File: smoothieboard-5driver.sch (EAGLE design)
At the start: 309 parts, among them IC1 LPC1769, IC10 LM1117-3.3V, IC11 78L12F, IC12 A4982, IC13 R-78E-5.0, IC14 TC4427, IC15 TC4427, IC2 A4982, IC3 A4982, IC4 MCP44X1, IC5 A4982, IC6 A4982, IC9 MCP44X1, J10 POWER_JACKSMD, Q1 BSL207SP, Q10 SUD50P04-08-GE3, Q2 12MHz, Q3 25MHz, Q4 ZXMN4A06, Q5 AOT240L, Q6 AOT240L, Q7 AOT240L, Q8 ZXMN4A06, Q9 ZXMN4A06, U1 USD-SOCKETNEW, X14 USBPTH

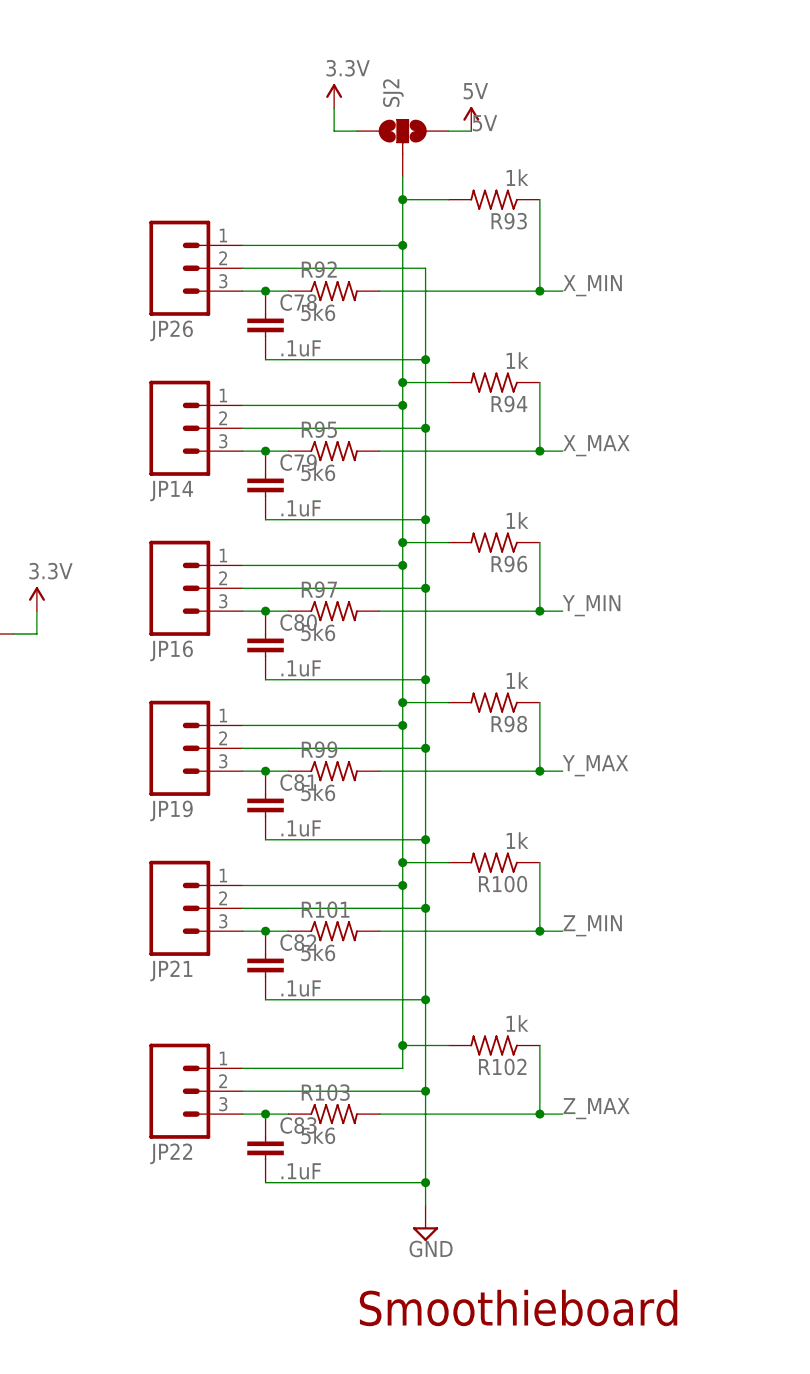
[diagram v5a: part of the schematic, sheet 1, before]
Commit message: fix endstop input ESD protection
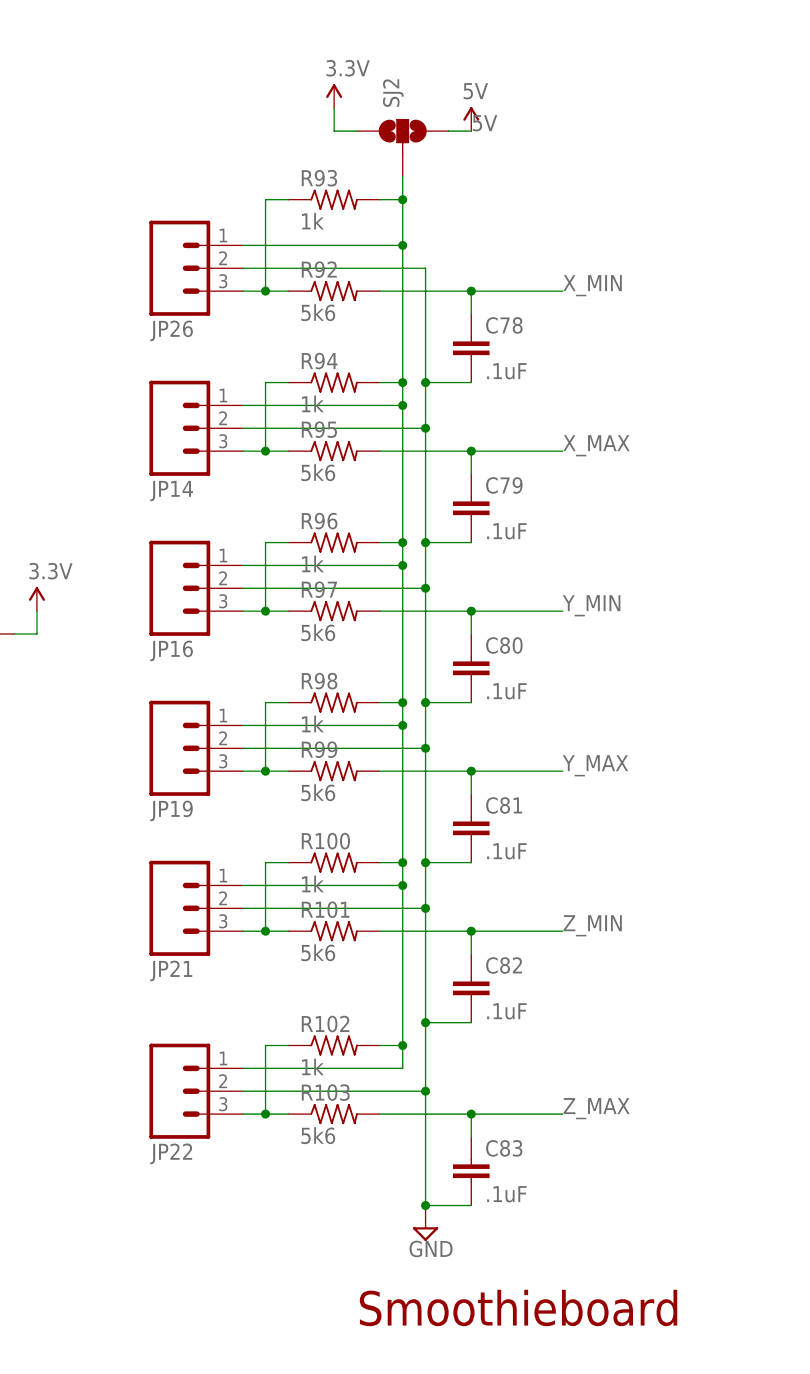
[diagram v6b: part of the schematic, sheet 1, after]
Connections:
- net N$114: now also R94.1; no longer C79.1
- net N$116: now also R96.1; no longer C80.1
- net N$117: now also R98.1; no longer C81.1
- net N$118: now also R102.1; no longer C83.1
- net N$119: now also R100.1; no longer C82.1
- net N$122: now also R93.1; no longer C78.1
- net X_MAX: now also C79.1; no longer R94.1
- net X_MIN: now also C78.1; no longer R93.1
- net Y_MAX: now also C81.1; no longer R98.1
- net Y_MIN: now also C80.1; no longer R96.1
- net Z_MAX: now also C83.1; no longer R102.1
- net Z_MIN: now also C82.1; no longer R100.1
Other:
- moved on the sheet: C78, C79, C80, C81, C82, C83, R100, R102, R93, R94, R96, R98

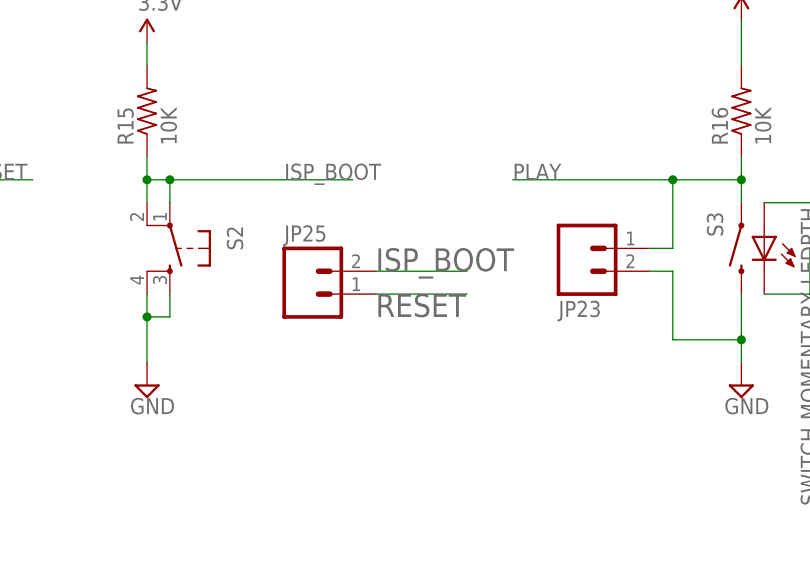
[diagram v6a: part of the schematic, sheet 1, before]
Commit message: lots of silk including pinouts on the bottom
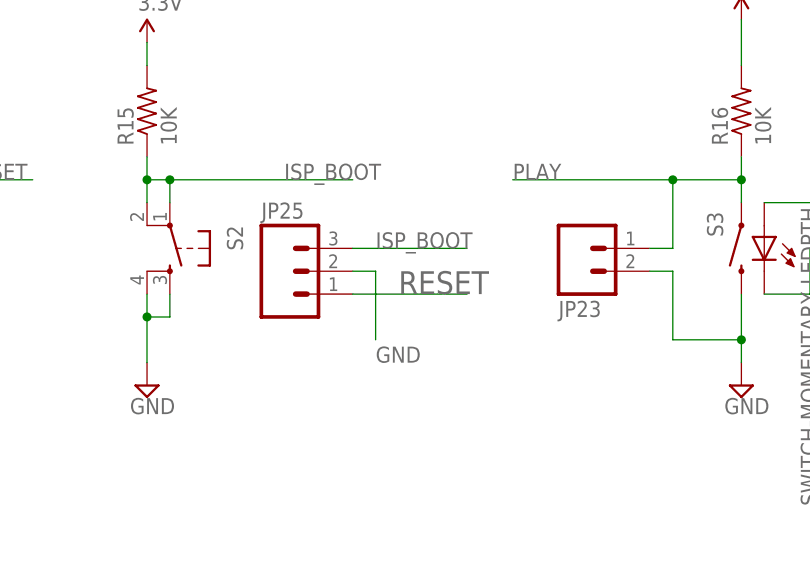
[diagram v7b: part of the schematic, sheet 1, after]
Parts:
- JP25: device SparkFun:M02PTH -> SparkFun-Connectors:M03PTH
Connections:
- net GND: now also JP25.2
- net ISP_BOOT: now also JP25.3; no longer JP25.2
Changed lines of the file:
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@@
 <?xml version="1.0" encoding="utf-8"?>
 <!DOCTYPE eagle SYSTEM "eagle.dtd">
-<eagle version="6.2">
+<eagle version="6.3">
 <drawing>
 <settings>
@@
 <part name="P+11" library="SparkFun" deviceset="3.3V" device=""/>
 <part name="SUPPLY32" library="supply2" deviceset="GND" device=""/>
-<part name="JP25" library="SparkFun" deviceset="M02" device="PTH"/>
+<part name="JP25" library="SparkFun-Connectors" deviceset="M03" device="PTH"/>
 <part name="JP24" library="SparkFun" deviceset="M02" device="PTH"/>
 <part name="JP23" library="SparkFun" deviceset="M02" device="PTH"/>
@@
 <instance part="P+11" gate="G$1" x="76.2" y="246.38"/>
 <instance part="SUPPLY32" gate="GND" x="76.2" y="220.98"/>
-<instance part="JP25" gate="G$1" x="137.16" y="17.78"/>
+<instance part="JP25" gate="G$1" x="134.62" y="20.32"/>
 <instance part="JP24" gate="G$1" x="210.82" y="22.86" rot="R180"/>
 <instance part="JP23" gate="G$1" x="167.64" y="22.86" rot="MR180"/>
@@
 <pinref part="JP33" gate="G$1" pin="5"/>
 </segment>
+<segment>
+<wire x1="142.24" y1="20.32" x2="144.78" y2="20.32" width="0.1524" layer="91"/>
+<pinref part="JP25" gate="G$1" pin="2"/>
+<wire x1="144.78" y1="12.7" x2="144.78" y2="20.32" width="0.1524" layer="91"/>
+<label x="144.78" y="10.16" size="1.778" layer="95"/>
+</segment>
 </net>
 <net name="3.3V" class="0">
@@
 </segment>
 <segment>
-<wire x1="144.78" y1="17.78" x2="154.94" y2="17.78" width="0.1524" layer="91"/>
-<label x="144.78" y="15.24" size="2.54" layer="95"/>
+<wire x1="142.24" y1="17.78" x2="154.94" y2="17.78" width="0.1524" layer="91"/>
+<label x="147.32" y="17.78" size="2.54" layer="95"/>
 <pinref part="JP25" gate="G$1" pin="1"/>
 </segment>
@@
 </segment>
 <segment>
-<wire x1="144.78" y1="20.32" x2="154.94" y2="20.32" width="0.1524" layer="91"/>
-<label x="144.78" y="20.32" size="2.54" layer="95"/>
-<pinref part="JP25" gate="G$1" pin="2"/>
-</segment>
-</net>
+<pinref part="JP25" gate="G$1" pin="3"/>
+<wire x1="154.94" y1="22.86" x2="142.24" y2="22.86" width="0.1524" layer="91"/>
+<label x="144.78" y="22.86" size="1.778" layer="95"/>
+</segment>
+</net>

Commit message: Update to v1.1
Board updated to v1.1. Also added changelog.txt and other some other
files needed for more complete license compliance.
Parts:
- added C84: 100uF, SparkFun-Capacitors:CAP_POLD
- added D7, D8, D9: MBRA210LT3, microbuilder:DIODESMA
- added JP13, JP36: (no value), SparkFun:JUMPER-2SMD-NC
- added JP35: (no value), SparkFun:M02PTH
- added U$11: FR000001, OSHWA:CERT-SMALL
- added U$12: FR000001, OSHWA:CERT-MEDIUM
- C63: device SparkFun:CAP_POLD -> SparkFun-Capacitors:CAP_POLE
- IC12, IC2, IC3, IC5, IC6: value A4982 -> A5984
- R65, R66, R67, R68, R84, R85: value 5.6K -> 8.2K
- R78: value 2.2K -> 8.2K
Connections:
- removed net 5VREG: C76.1, D6.A, IC13.VO
- new net MS3: IC12.VDD, IC2.VDD, IC3.VDD, IC5.VDD, IC6.VDD, JP36.1
- new net TH4_P: C24.+, JP13.2, RN1D.2
- new net VBBREG: C77.1, D6.C, IC13.VI
- net 3.3V: now also JP36.2; no longer IC12.VDD, IC2.VDD, IC3.VDD, IC5.VDD, IC6.VDD
- net 5V: now also C76.1, C84.+, IC13.VO; no longer D6.C
- net AGND: now also JP35.2
- net AVCC: now also JP35.1
- net GND: now also C84.-
- net N$111: now also D5.A; no longer D5.C
- net N$18: now also D8.A
- net N$52: now also D9.A
- net N$88: now also D7.A
- net SMALL_MOSFET_POWER: now also D7.C, D8.C
- net TH4: now also JP13.1; no longer C24.+, RN1D.2
- net VBB: now also D5.C, D6.A, D9.C; no longer C77.1, D5.A, IC13.VI
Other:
- moved on the sheet: D5, J8, X7
